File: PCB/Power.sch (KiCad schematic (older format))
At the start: 18 parts, among them J1 B2B-PH-K-S(LF)(SN), J2 B3B-PH-K-S(LF)(SN), Q1 DMG2307L-7, Q2 DMG2307L-7, U1 BQ24210DQCT, U2 AZ1117CR-3.3TRG1_1

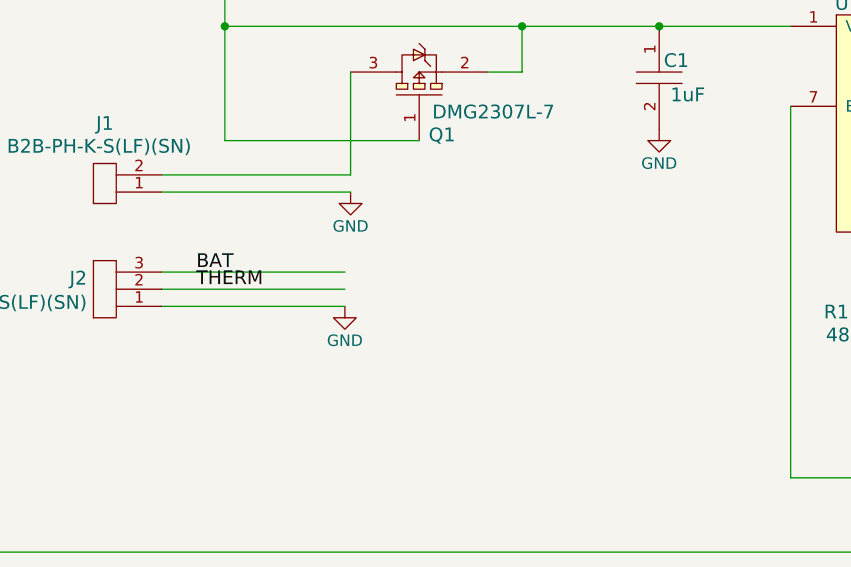
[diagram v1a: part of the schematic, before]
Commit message: Switch
Power switch added for switching board off for storage and shipping.
Power supply circuit routing revised and updated.
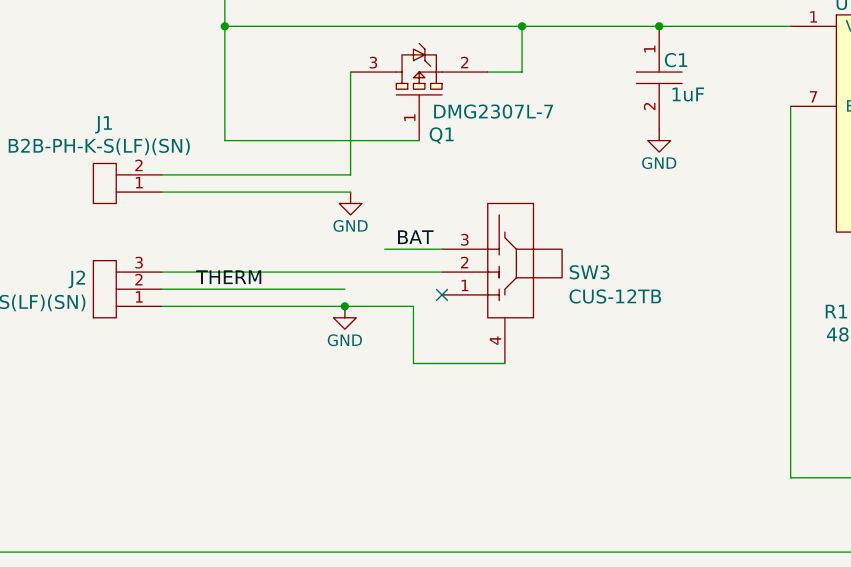
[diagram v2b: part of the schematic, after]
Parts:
- added SW3: CUS-12TB, PCB_Footprints:CUS-12TB, symbol CUS-12TB
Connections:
- wire segments 41 -> 44
- no-connect marks 0 -> 1
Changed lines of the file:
@@
 $EndComp
 Wire Wire Line
-	2725 4125 1925 4125
+	1925 4125 3025 4125
 Wire Wire Line
 	1925 4050 2725 4050
 Wire Wire Line
-	1925 3975 2725 3975
-Text Label 2075 3975 0    60   ~ 0
+	1925 3975 3150 3975
+Text Label 2950 3875 0    60   ~ 0
 BAT
 Text Label 2075 4050 0    60   ~ 0
@@
 Text HLabel 975  5200 0    60   Output ~ 0
 BAT_VOLT
+$Comp
+L CUS-12TB SW3
+U 1 1 58127F98
+P 3425 3975
+F 0 "SW3" V 3422 3697 60  0000 R CNN
+F 1 "CUS-12TB" V 3316 3697 60  0000 R CNN
+F 2 "PCB_Footprints:CUS-12TB" H 2675 4950 60  0001 C CNN
+F 3 "http://www.nidec-copal-electronics.com/e/catalog/switch/cus.pdf" H 2775 5050 60  0001 C CNN
+F 4 "0.45329 @ 1000" H 2875 5150 60  0001 C CNN "Cost"
+F 5 "24 Oct 2016" H 2975 5250 60  0001 C CNN "Date Created"
+F 6 "24 Oct 2016" H 3075 5350 60  0001 C CNN "Date Modifed"
+F 7 "Adam Vadala-Roth" H 3175 5450 60  0001 C CNN "Designer"
+F 8 "2mm" H 3275 5550 60  0001 C CNN "Height"
+F 9 "Yes" H 3375 5650 60  0001 C CNN "RHoS?"
+F 10 "Copal Electronics Inc." H 3475 5750 60  0001 C CNN "MFR"
+F 11 "CUS-12TB" H 3575 5850 60  0001 C CNN "MFR#"
+F 12 "SMT/SMD" H 3675 5950 60  0001 C CNN "Mounting"
+F 13 "3" H 3775 6050 60  0001 C CNN "Pin Count#"
+F 14 "Active" H 3875 6150 60  0001 C CNN "Status"
+F 15 "N/A" H 3975 6250 60  0001 C CNN "Tolerance"
+F 16 "SMT Slider switch SPDT" H 4075 6350 60  0001 C CNN "Type"
+F 17 "50V 100mA" H 4175 6450 60  0001 C CNN "Voltage"
+F 18 "N/A" H 4725 6450 60  0001 C CNN "Wattage"
+F 19 "N/A" H 3125 4850 60  0001 C CNN "Componen-Value"
+F 20 "Slide Switch SPDT Surface Mount, Right Angle" H 4925 6650 60  0001 C CNN "Description"
+	1    3425 3975
+	0    -1   -1   0
+$EndComp
+Wire Wire Line
+	3150 3875 2900 3875
+Wire Wire Line
+	3025 4125 3025 4375
+Wire Wire Line
+	3025 4375 3425 4375
+Connection ~ 2725 4125
+NoConn ~ 3150 4075
 $EndSCHEMATC

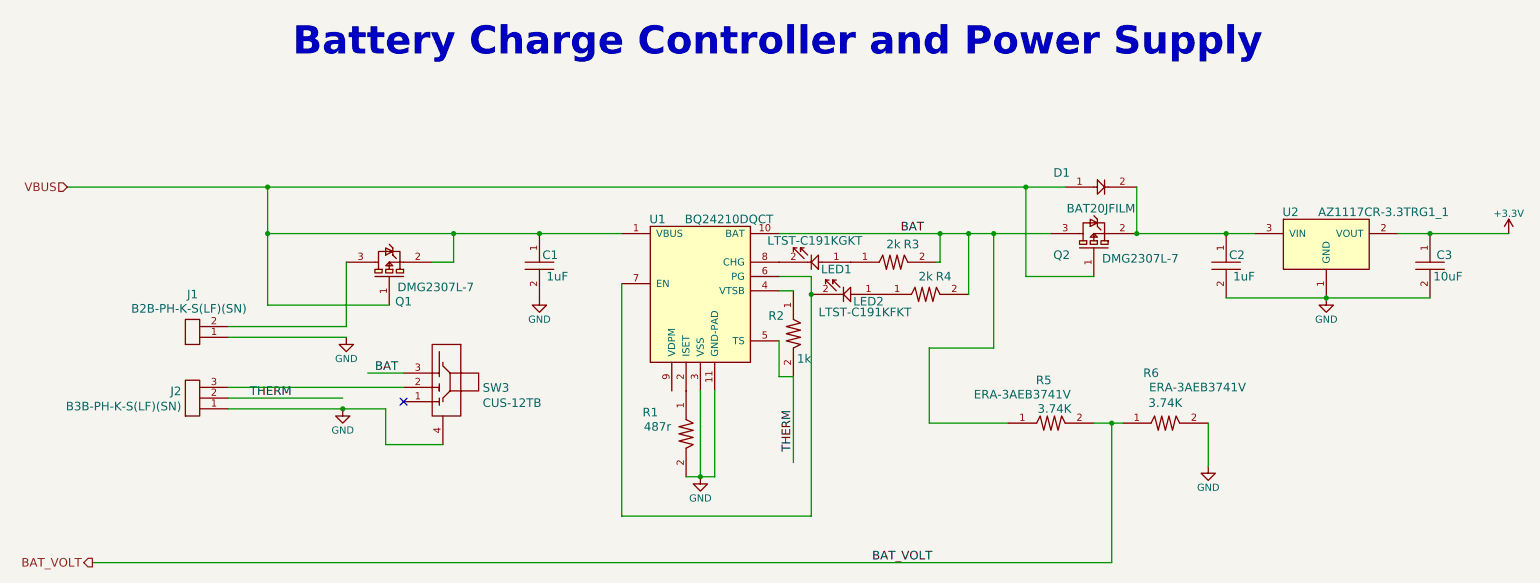
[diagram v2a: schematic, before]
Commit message: Power Switch Revision
Power switch and power supply topology revised. New microchip LDO from
Ventor replaces old LDO, power switch not toggles LDO shutdown enable
for turing Aria on and off.
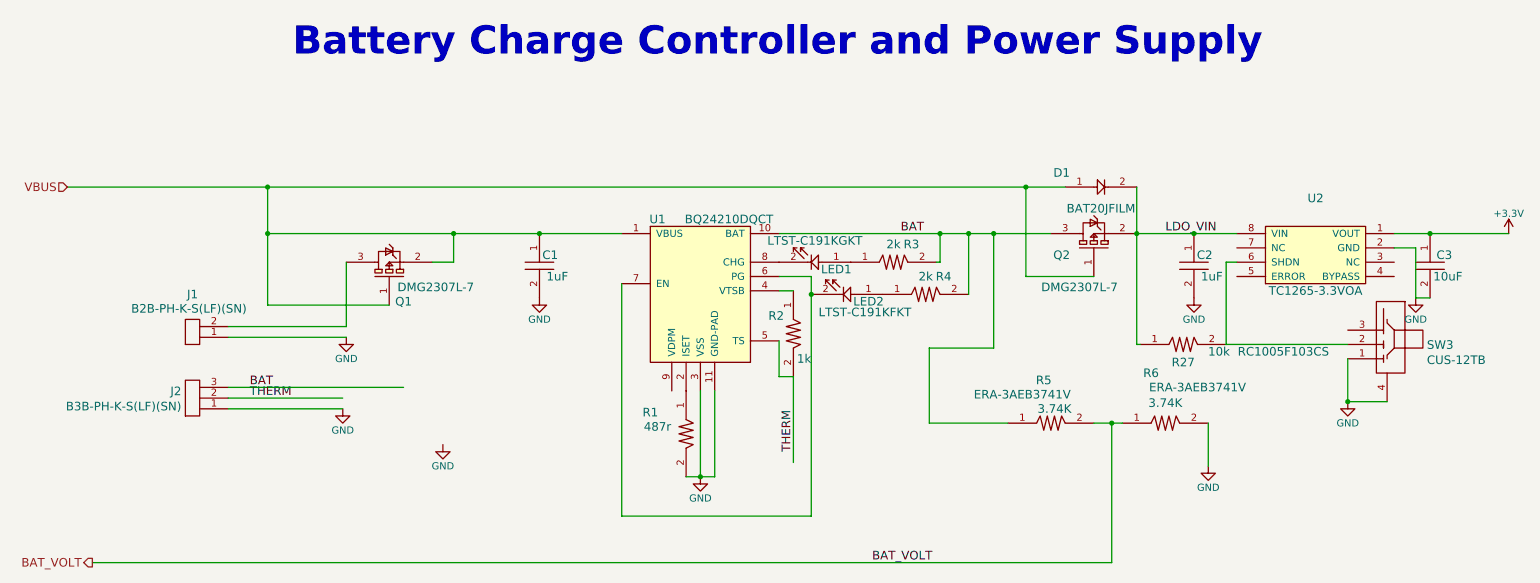
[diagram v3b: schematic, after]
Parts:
- removed U2: AZ1117CR-3.3TRG1_1, PCB_Footprints:AZ1117CR-3.3TRG1, symbol AZ1117CR-3.3TRG1_1
- added R27: RC1005F103CS, PCB_Footprints:R0402, symbol RC1005F103CS
- added U2: TC1265-3.3VOA, PCB_Footprints:TC1265-3.3VOA, symbol TC1265-3.3VOA
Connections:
- net labels added: LDO_VIN
- wire segments 44 -> 50
- no-connect marks 1 -> 0
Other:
- moved on the sheet: C2
